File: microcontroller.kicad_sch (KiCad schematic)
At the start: 50 parts, among them J1 Conn_01x06, J2 Conn_01x06, J3 47219-2001, SW1 SW_Push, U1 TPS7B88, U2 MCP1700x-330xxMB, U3 STM32F103C8Tx, U4 SN65HVD1050D, U5 TCA9535PWR, Y1 8M, Y2 32.768k

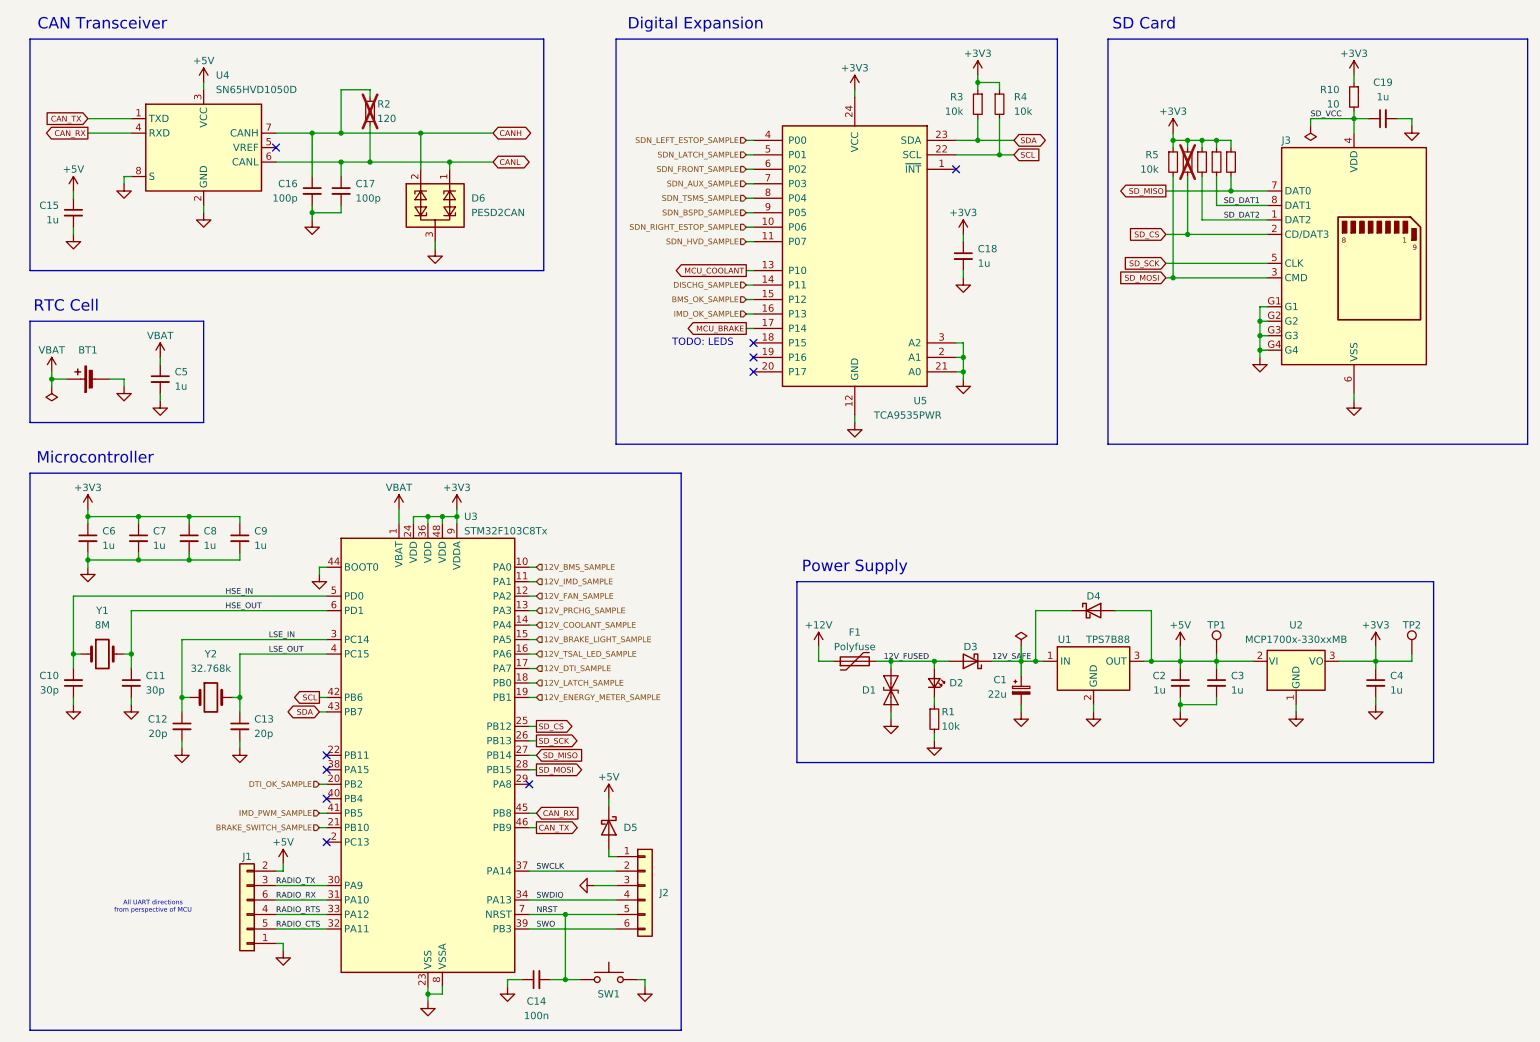
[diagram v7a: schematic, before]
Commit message: *: Add CAN test points
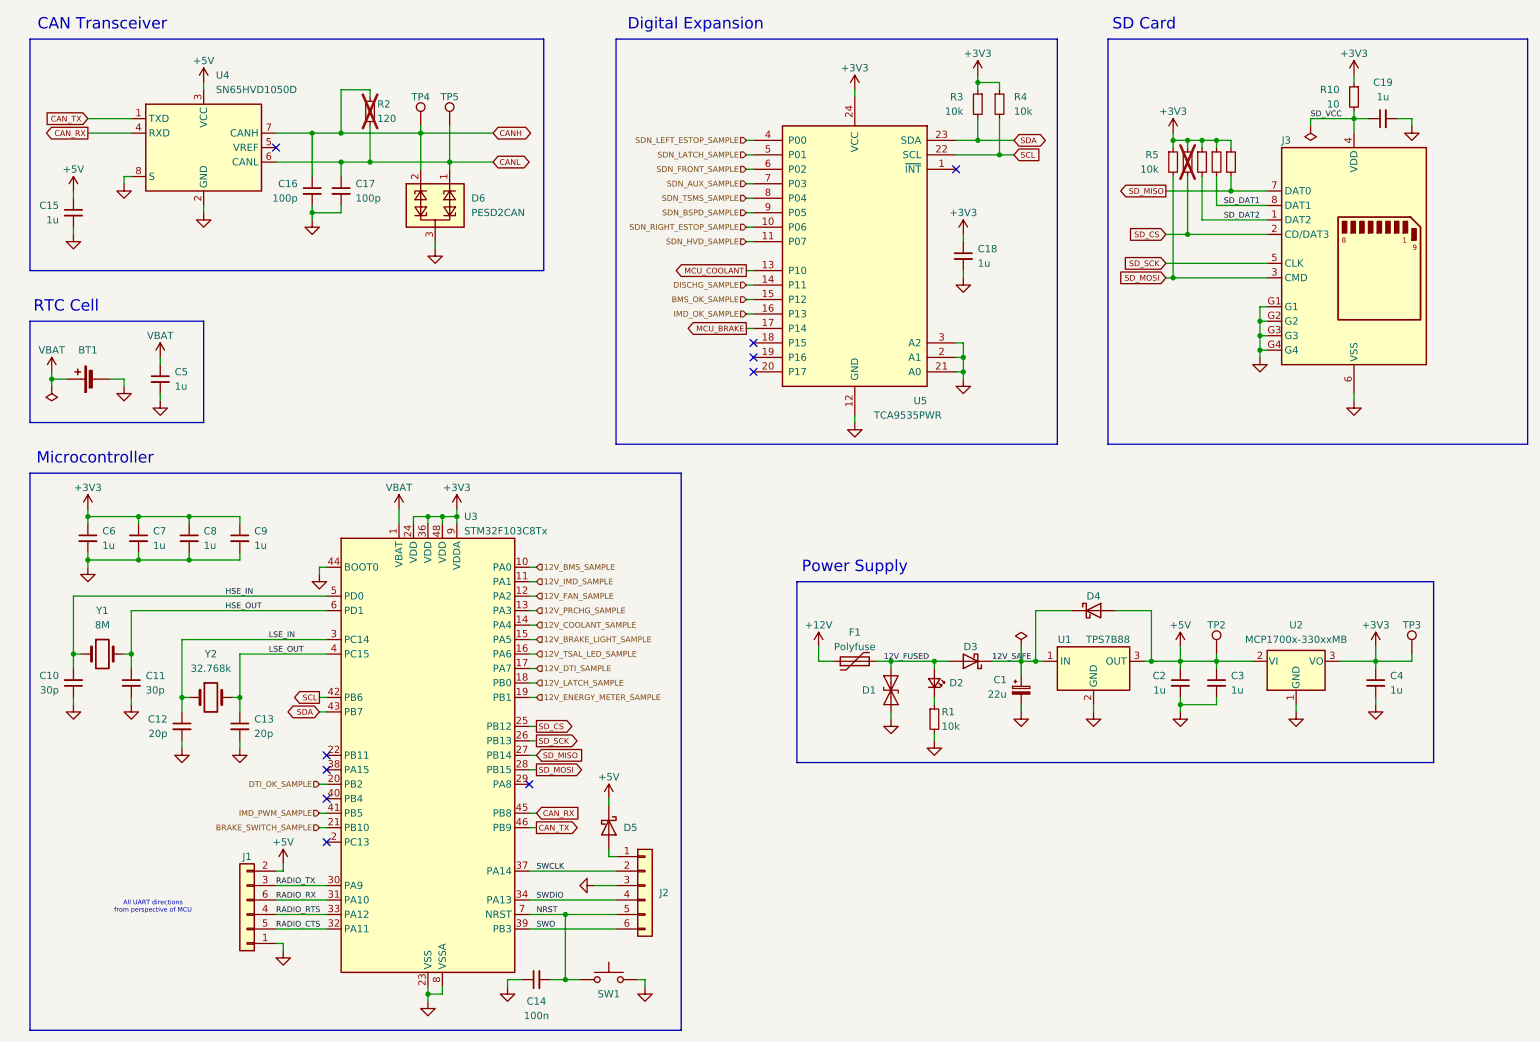
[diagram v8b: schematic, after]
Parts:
- added TP4, TP5: TestPoint, TestPoint:TestPoint_THTPad_D2.0mm_Drill1.0mm, symbol Connector:TestPoint
- renumbered TP1 to TP2, TP2 to TP3
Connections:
- net CANH: now also TP4.1
- net CANL: now also TP5.1
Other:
- note removed: "TODO: LEDS"
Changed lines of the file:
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@@
 		)
 	)
-	(text "TODO: LEDS"
-		(exclude_from_sim no)
-		(at 134.62 73.66 0)
-		(effects
-			(font
-				(size 1.27 1.27)
-			)
-		)
-	)
 	(text "CAN Transceiver"
 		(exclude_from_sim no)
@@
 	)
 	(no_connect
-		(at 143.51 73.66)
+		(at 143.51 76.2)
 	)
 	(no_connect
-		(at 143.51 78.74)
+		(at 143.51 73.66)
 	)
 	(no_connect
@@
 	)
 	(no_connect
-		(at 143.51 76.2)
-	)
-	(no_connect
 		(at 179.07 43.18)
 	)
@@
 	)
 	(no_connect
+		(at 143.51 78.74)
+	)
+	(no_connect
 		(at 68.58 148.59)
 	)
@@
 	(wire
 		(pts
+			(xy 90.17 35.56) (xy 90.17 41.91)
+		)
+		(stroke
+			(width 0)
+			(type default)
+		)
+	)
+	(wire
+		(pts
 			(xy 252.73 129.54) (xy 259.08 129.54)
 		)
@@
 	(wire
 		(pts
+			(xy 85.09 35.56) (xy 85.09 36.83)
+		)
+		(stroke
+			(width 0)
+			(type default)
+		)
+	)
+	(wire
+		(pts
 			(xy 71.12 50.8) (xy 66.04 50.8)
 		)
@@
 		(on_board yes)
 		(dnp no)
-		(property "Reference" "TP2"
+		(property "Reference" "TP3"
 			(at 259.08 123.19 0)
 			(effects
@@
 			(project "rear_distribution"
 				(path "/f2809c69-a8f9-4542-bde7-ba954770c514/441bb5a1-b38a-4f03-91d4-c403979ff70d"
-					(reference "TP2")
+					(reference "TP3")
 					(unit 1)
 				)
@@
 		(on_board yes)
 		(dnp no)
-		(property "Reference" "TP1"
+		(property "Reference" "TP2"
 			(at 224.79 123.19 0)
 			(effects
@@
 			(project "rear_distribution"
 				(path "/f2809c69-a8f9-4542-bde7-ba954770c514/441bb5a1-b38a-4f03-91d4-c403979ff70d"
-					(reference "TP1")
+					(reference "TP2")
 					(unit 1)
 				)
@@
 	)
 	(symbol
+		(lib_id "Connector:TestPoint")
+		(at 85.09 35.56 0)
+		(unit 1)
+		(exclude_from_sim no)
+		(in_bom yes)
+		(on_board yes)
+		(dnp no)
+		(property "Reference" "TP4"
+			(at 85.09 30.48 0)
+			(effects
+				(font
+					(size 1.27 1.27)
+				)
+			)
+		)
+		(property "Value" "TestPoint"
+			(at 87.63 33.5279 0)
+			(effects
+				(font
+					(size 1.27 1.27)
+				)
+				(justify left)
+				(hide yes)
+			)
+		)
+		(property "Footprint" "TestPoint:TestPoint_THTPad_D2.0mm_Drill1.0mm"
+			(at 90.17 35.56 0)
+			(effects
+				(font
+					(size 1.27 1.27)
+				)
+				(hide yes)
+			)
+		)
+		(property "Datasheet" "~"
+			(at 90.17 35.56 0)
+			(effects
+				(font
+					(size 1.27 1.27)
+				)
+				(hide yes)
+			)
+		)
+		(property "Description" "test point"
+			(at 85.09 35.56 0)
+			(effects
+				(font
+					(size 1.27 1.27)
+				)
+				(hide yes)
+			)
+		)
+		(pin "1"
+		)
+		(instances
+			(project "rear_distribution"
+				(path "/f2809c69-a8f9-4542-bde7-ba954770c514/441bb5a1-b38a-4f03-91d4-c403979ff70d"
+					(reference "TP4")
+					(unit 1)
+				)
+			)
+		)
+	)
+	(symbol
 		(lib_id "power:+3V3")
 		(at 248.92 26.67 0)
@@
 					(unit 1)
 				)
+			)
+		)
+	)
+	(symbol
+		(lib_id "Connector:TestPoint")
+		(at 90.17 35.56 0)
+		(unit 1)
+		(exclude_from_sim no)
+		(in_bom yes)
+		(on_board yes)
+		(dnp no)
+		(property "Reference" "TP5"
+			(at 90.17 30.48 0)
+			(effects
+				(font
+					(size 1.27 1.27)
+				)
+			)
+		)
+		(property "Value" "TestPoint"
+			(at 92.71 33.5279 0)
+			(effects
+				(font
+					(size 1.27 1.27)
+				)
+				(justify left)
+				(hide yes)
+			)
+		)
+		(property "Footprint" "TestPoint:TestPoint_THTPad_D2.0mm_Drill1.0mm"
+			(at 95.25 35.56 0)
+			(effects
+				(font
+					(size 1.27 1.27)
+				)
+				(hide yes)
+			)
+		)
+		(property "Datasheet" "~"
+			(at 95.25 35.56 0)
+			(effects
+				(font
+					(size 1.27 1.27)
+				)
+				(hide yes)
+			)
+		)
+		(property "Description" "test point"
+			(at 90.17 35.56 0)
+			(effects
+				(font
+					(size 1.27 1.27)
+				)
+				(hide yes)
+			)
+		)
+		(pin "1"
+		)
+		(instances
+			(project "rear_distribution"
+				(path "/f2809c69-a8f9-4542-bde7-ba954770c514/441bb5a1-b38a-4f03-91d4-c403979ff70d"
+					(reference "TP5")
+					(unit 1)
+				)
